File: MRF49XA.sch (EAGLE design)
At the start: 46 parts, among them J1 AVR_SPI_PRG_6NS, Q1 10Mhz, U1 ATSHA204, U2 ANT1204F002R0433A, U4 MCP73831, Y1 16MHZ

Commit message: PDF
Added PDF of the circuit.
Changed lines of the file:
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@@
 <net name="N$18" class="0">
 <segment>
-<wire x1="-121.92" y1="109.22" x2="147.32" y2="109.22" width="0.1524" layer="91"/>
-<wire x1="147.32" y1="109.22" x2="147.32" y2="10.16" width="0.1524" layer="91"/>
-<wire x1="147.32" y1="10.16" x2="-127" y2="10.16" width="0.1524" layer="91"/>
+<wire x1="-127" y1="109.22" x2="152.4" y2="109.22" width="0.1524" layer="91"/>
+<wire x1="152.4" y1="109.22" x2="152.4" y2="10.16" width="0.1524" layer="91"/>
+<wire x1="152.4" y1="10.16" x2="-127" y2="10.16" width="0.1524" layer="91"/>
 <wire x1="-127" y1="10.16" x2="-127" y2="109.22" width="0.1524" layer="91"/>
-<wire x1="-127" y1="109.22" x2="-121.92" y2="109.22" width="0.1524" layer="91"/>
 </segment>
 </net>

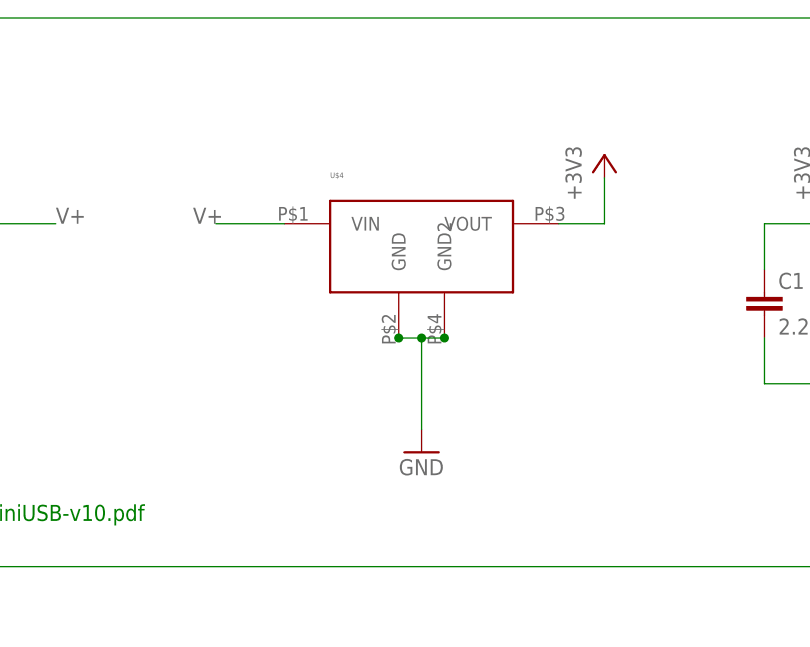
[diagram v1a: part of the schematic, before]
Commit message: Linear regulator changed
Changed it. Cheaper. Plus the other one would have blown up my circuit.
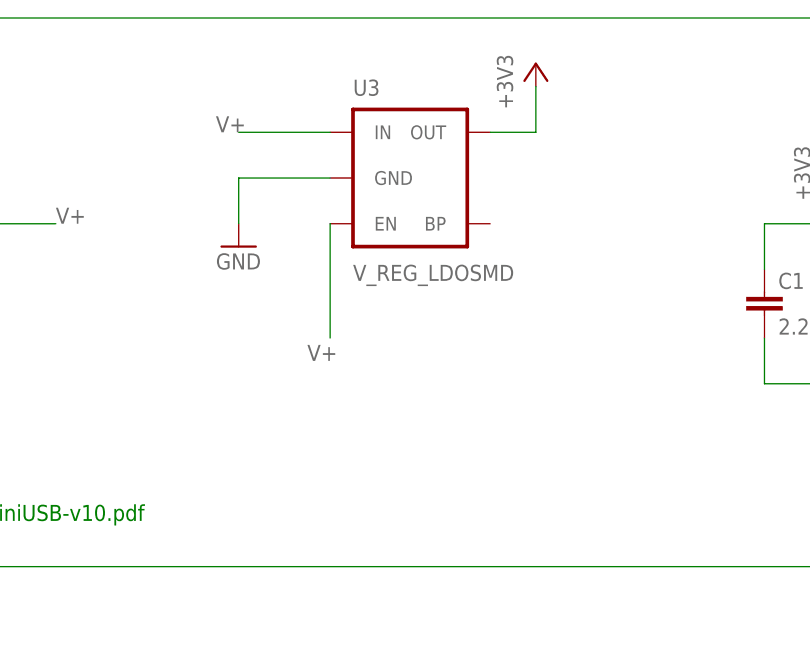
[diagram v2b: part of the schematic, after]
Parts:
- removed U$4: (no value), TestLibrary:TLV1117
- added U3: V_REG_LDOSMD, SparkFun-PowerIC:V_REG_LDOSMD
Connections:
- net +3V3: now also U3.OUT; no longer U$4.VOUT
- net GND: now also U3.GND; no longer U$4.GND, U$4.GND2
- net V+: now also U3.EN, U3.IN; no longer U$4.VIN
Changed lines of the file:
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@@
 <part name="TP3" library="testpad" deviceset="TP" device="TP08R"/>
 <part name="Y1" library="SparkFun-FreqCtrl" deviceset="RESONATOR" device="8MHZ" value="16MHZ"/>
-<part name="U$4" library="TestLibrary" deviceset="TLV1117" device=""/>
 <part name="L2" library="SparkFun-Passives" deviceset="INDUCTOR" device="0603"/>
 <part name="L1" library="SparkFun-Passives" deviceset="INDUCTOR" device="0603"/>
@@
 <part name="C9" library="SparkFun-Passives" deviceset="CAP" device="0603-CAP"/>
 <part name="U2" library="TestLibrary" deviceset="ANT1204F002R0433A" device=""/>
+<part name="U3" library="SparkFun-PowerIC" deviceset="V_REG_LDO" device="SMD"/>
 </parts>
 <sheets>
@@
 <instance part="C4" gate="G$1" x="-43.18" y="60.96"/>
 <instance part="+3V1" gate="G$1" x="83.82" y="167.64"/>
-<instance part="+3V3" gate="G$1" x="58.42" y="167.64"/>
+<instance part="+3V3" gate="G$1" x="50.8" y="177.8"/>
 <instance part="+3V4" gate="G$1" x="-66.04" y="83.82"/>
 <instance part="C8" gate="G$1" x="-50.8" y="53.34"/>
 <instance part="U$1" gate="G$1" x="-86.36" y="68.58" smashed="yes"/>
-<instance part="GND3" gate="1" x="38.1" y="134.62"/>
+<instance part="GND3" gate="1" x="17.78" y="157.48"/>
 <instance part="GND4" gate="1" x="83.82" y="134.62"/>
 <instance part="GND6" gate="1" x="-66.04" y="35.56"/>
@@
 </instance>
 <instance part="Y1" gate="G$1" x="195.58" y="53.34" rot="R270"/>
-<instance part="U$4" gate="G$1" x="40.64" y="144.78"/>
 <instance part="L2" gate="G$1" x="68.58" y="58.42"/>
 <instance part="L1" gate="G$1" x="68.58" y="78.74"/>
@@
 <instance part="C9" gate="G$1" x="91.44" y="40.64"/>
 <instance part="U2" gate="ANTENNA" x="127" y="71.12" rot="MR180"/>
+<instance part="U3" gate="G$1" x="38.1" y="165.1"/>
 </instances>
 <busses>
@@
 <segment>
 <pinref part="+3V3" gate="G$1" pin="+3V3"/>
-<wire x1="58.42" y1="165.1" x2="58.42" y2="160.02" width="0.1524" layer="91"/>
-<pinref part="U$4" gate="G$1" pin="VOUT"/>
-<wire x1="58.42" y1="160.02" x2="53.34" y2="160.02" width="0.1524" layer="91"/>
+<wire x1="50.8" y1="175.26" x2="50.8" y2="170.18" width="0.1524" layer="91"/>
+<wire x1="50.8" y1="170.18" x2="45.72" y2="170.18" width="0.1524" layer="91"/>
+<pinref part="U3" gate="G$1" pin="OUT"/>
 </segment>
 <segment>
@@
 </segment>
 <segment>
-<label x="12.7" y="160.02" size="1.778" layer="95"/>
-<pinref part="U$4" gate="G$1" pin="VIN"/>
-<wire x1="15.24" y1="160.02" x2="22.86" y2="160.02" width="0.1524" layer="91"/>
+<label x="15.24" y="170.18" size="1.778" layer="95"/>
+<wire x1="17.78" y1="170.18" x2="27.94" y2="170.18" width="0.1524" layer="91"/>
+<pinref part="U3" gate="G$1" pin="IN"/>
+</segment>
+<segment>
+<label x="25.4" y="144.78" size="1.778" layer="95"/>
+<wire x1="27.94" y1="147.32" x2="27.94" y2="160.02" width="0.1524" layer="91"/>
+<pinref part="U3" gate="G$1" pin="EN"/>
 </segment>
 </net>
@@
 </segment>
 <segment>
-<pinref part="GND3" gate="1" pin="GND"/>
-<wire x1="38.1" y1="137.16" x2="38.1" y2="147.32" width="0.1524" layer="91"/>
-<pinref part="U$4" gate="G$1" pin="GND"/>
-<pinref part="U$4" gate="G$1" pin="GND2"/>
-<wire x1="35.56" y1="147.32" x2="38.1" y2="147.32" width="0.1524" layer="91"/>
-<junction x="38.1" y="147.32"/>
-<wire x1="38.1" y1="147.32" x2="40.64" y2="147.32" width="0.1524" layer="91"/>
-<junction x="35.56" y="147.32"/>
-<junction x="40.64" y="147.32"/>
-</segment>
-<segment>
 <pinref part="C9" gate="G$1" pin="2"/>
 <wire x1="91.44" y1="38.1" x2="91.44" y2="35.56" width="0.1524" layer="91"/>
 <label x="88.9" y="33.02" size="1.778" layer="95"/>
 </segment>
+<segment>
+<pinref part="GND3" gate="1" pin="GND"/>
+<wire x1="17.78" y1="160.02" x2="17.78" y2="165.1" width="0.1524" layer="91"/>
+<pinref part="U3" gate="G$1" pin="GND"/>
+<wire x1="17.78" y1="165.1" x2="27.94" y2="165.1" width="0.1524" layer="91"/>
+</segment>
 </net>

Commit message: Capacitor and V reg
Added Aref capacitor. Changed voltage regulator.
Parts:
- added C10: 0.1uF, SparkFun-Capacitors:0.1UF-25V-5%(0603)
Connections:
- new net AREF: C10.1, U$3.AREF
- net GND: now also C10.2
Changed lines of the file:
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@@
 <part name="U2" library="TestLibrary" deviceset="ANT1204F002R0433A" device=""/>
 <part name="U3" library="SparkFun-PowerIC" deviceset="V_REG_LDO" device="SMD"/>
+<part name="C10" library="SparkFun-Capacitors" deviceset="0.1UF-25V-5%(0603)" device="" value="0.1uF"/>
+<part name="GND2" library="supply1" deviceset="GND" device=""/>
 </parts>
 <sheets>
@@
 <instance part="U2" gate="ANTENNA" x="127" y="71.12" rot="MR180"/>
 <instance part="U3" gate="G$1" x="38.1" y="165.1"/>
+<instance part="C10" gate="G$1" x="175.26" y="91.44"/>
+<instance part="GND2" gate="1" x="175.26" y="81.28"/>
 </instances>
 <busses>
@@
 <wire x1="17.78" y1="165.1" x2="27.94" y2="165.1" width="0.1524" layer="91"/>
 </segment>
+<segment>
+<pinref part="C10" gate="G$1" pin="2"/>
+<pinref part="GND2" gate="1" pin="GND"/>
+<wire x1="175.26" y1="88.9" x2="175.26" y2="83.82" width="0.1524" layer="91"/>
+</segment>
 </net>
 <net name="N$5" class="0">
@@
 </segment>
 </net>
+<net name="AREF" class="0">
+<segment>
+<pinref part="C10" gate="G$1" pin="1"/>
+<wire x1="175.26" y1="96.52" x2="175.26" y2="99.06" width="0.1524" layer="91"/>
+<label x="175.26" y="99.06" size="1.778" layer="95"/>
+</segment>
+<segment>
+<pinref part="U$3" gate="G$1" pin="AREF"/>
+<wire x1="220.98" y1="88.9" x2="215.9" y2="88.9" width="0.1524" layer="91"/>
+<label x="213.36" y="88.9" size="1.778" layer="95"/>
+</segment>
+</net>

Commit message: V Regulators
Added a list of possible voltage regulators.
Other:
- note added: "ADP1712 MIC5259 MIC5205"
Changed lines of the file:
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@@
 <text x="167.64" y="7.62" size="1.778" layer="91">Processor</text>
 <text x="119.38" y="119.38" size="1.778" layer="91">Headers &amp; Test points</text>
+<text x="25.4" y="137.16" size="1.778" layer="91">ADP1712
+MIC5259
+MIC5205</text>
 </plain>
 <instances>
@@
 </schematic>
 </drawing>
+<compatibility>
+<note version="6.3" minversion="6.2.2" severity="warning">
+Since Version 6.2.2 text objects can contain more than one line,
+which will not be processed correctly with this version.
+</note>
+</compatibility>
 </eagle>

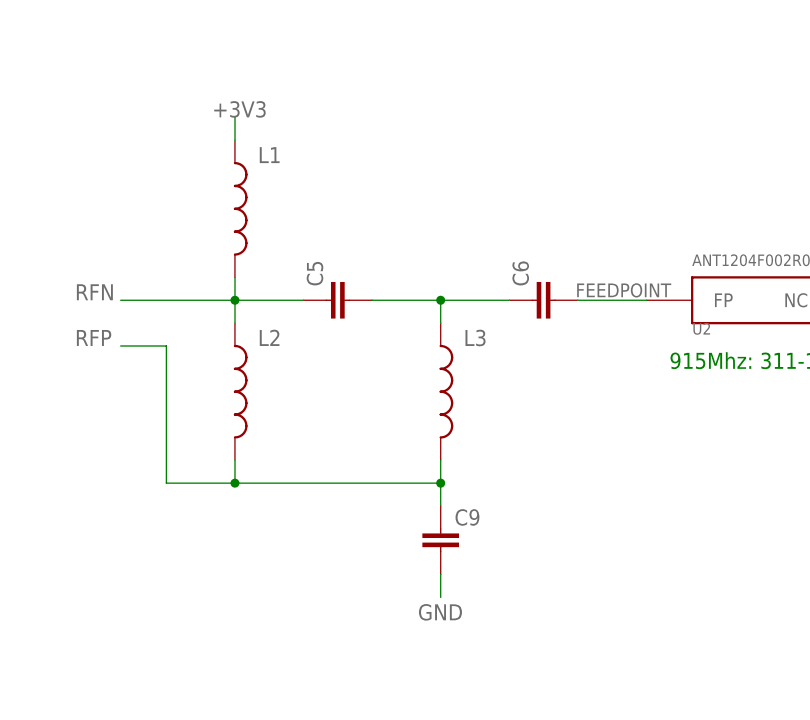
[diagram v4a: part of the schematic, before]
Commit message: BOM
Added BOM and values to antenna section
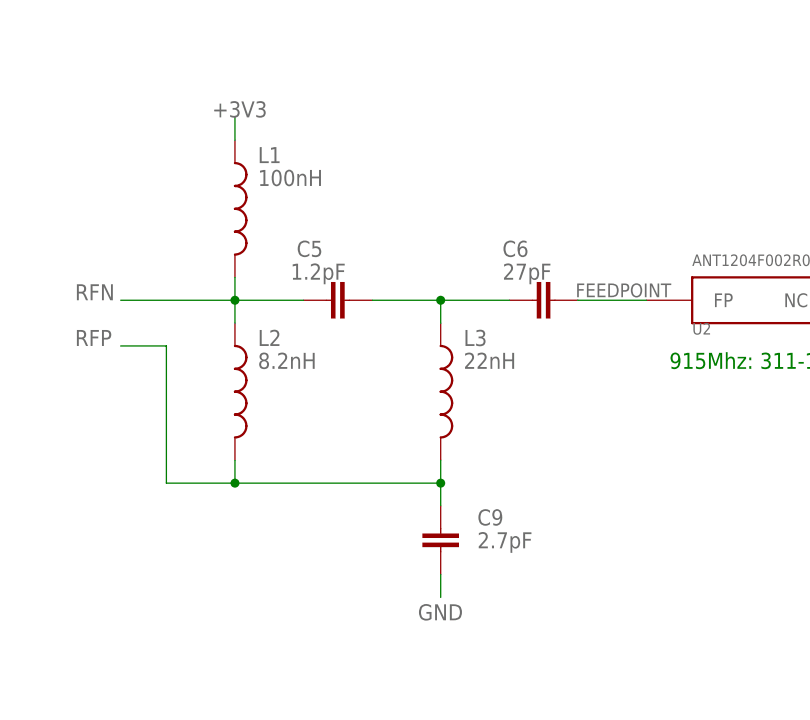
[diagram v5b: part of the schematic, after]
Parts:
- C5: value (none) -> 1.2pF
- C6: value (none) -> 27pF
- C9: value (none) -> 2.7pF
- L1: value (none) -> 100nH
- L2: value (none) -> 8.2nH
- L3: value (none) -> 22nH
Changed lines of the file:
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@@
 <part name="TP3" library="testpad" deviceset="TP" device="TP08R"/>
 <part name="Y1" library="SparkFun-FreqCtrl" deviceset="RESONATOR" device="8MHZ" value="16MHZ"/>
-<part name="L2" library="SparkFun-Passives" deviceset="INDUCTOR" device="0603"/>
-<part name="L1" library="SparkFun-Passives" deviceset="INDUCTOR" device="0603"/>
-<part name="L3" library="SparkFun-Passives" deviceset="INDUCTOR" device="0603"/>
-<part name="C5" library="SparkFun-Passives" deviceset="CAP" device="0603-CAP"/>
-<part name="C6" library="SparkFun-Passives" deviceset="CAP" device="0603-CAP"/>
-<part name="C9" library="SparkFun-Passives" deviceset="CAP" device="0603-CAP"/>
+<part name="L2" library="SparkFun-Passives" deviceset="INDUCTOR" device="0603" value="8.2nH"/>
+<part name="L1" library="SparkFun-Passives" deviceset="INDUCTOR" device="0603" value="100nH"/>
+<part name="L3" library="SparkFun-Passives" deviceset="INDUCTOR" device="0603" value="22nH"/>
+<part name="C5" library="SparkFun-Passives" deviceset="CAP" device="0603-CAP" value="1.2pF"/>
+<part name="C6" library="SparkFun-Passives" deviceset="CAP" device="0603-CAP" value="27pF"/>
+<part name="C9" library="SparkFun-Passives" deviceset="CAP" device="0603-CAP" value="2.7pF"/>
 <part name="U2" library="TestLibrary" deviceset="ANT1204F002R0433A" device=""/>
 <part name="U3" library="SparkFun-PowerIC" deviceset="V_REG_LDO" device="SMD"/>
@@
 </instance>
 <instance part="Y1" gate="G$1" x="195.58" y="53.34" rot="R270"/>
-<instance part="L2" gate="G$1" x="68.58" y="58.42"/>
-<instance part="L1" gate="G$1" x="68.58" y="78.74"/>
-<instance part="L3" gate="G$1" x="91.44" y="58.42"/>
-<instance part="C5" gate="G$1" x="81.28" y="68.58" rot="R90"/>
-<instance part="C6" gate="G$1" x="104.14" y="68.58" rot="R90"/>
-<instance part="C9" gate="G$1" x="91.44" y="40.64"/>
+<instance part="L2" gate="G$1" x="68.58" y="58.42" smashed="yes">
+<attribute name="NAME" x="71.12" y="63.5" size="1.778" layer="95"/>
+<attribute name="VALUE" x="71.12" y="60.96" size="1.778" layer="96"/>
+</instance>
+<instance part="L1" gate="G$1" x="68.58" y="78.74" smashed="yes">
+<attribute name="NAME" x="71.12" y="83.82" size="1.778" layer="95"/>
+<attribute name="VALUE" x="71.12" y="81.28" size="1.778" layer="96"/>
+</instance>
+<instance part="L3" gate="G$1" x="91.44" y="58.42" smashed="yes">
+<attribute name="NAME" x="93.98" y="63.5" size="1.778" layer="95"/>
+<attribute name="VALUE" x="93.98" y="60.96" size="1.778" layer="96"/>
+</instance>
+<instance part="C5" gate="G$1" x="81.28" y="68.58" smashed="yes" rot="R90">
+<attribute name="NAME" x="78.359" y="75.184" size="1.778" layer="95" rot="R180"/>
+<attribute name="VALUE" x="80.899" y="72.644" size="1.778" layer="96" rot="R180"/>
+</instance>
+<instance part="C6" gate="G$1" x="104.14" y="68.58" smashed="yes" rot="R90">
+<attribute name="NAME" x="101.219" y="75.184" size="1.778" layer="95" rot="R180"/>
+<attribute name="VALUE" x="103.759" y="72.644" size="1.778" layer="96" rot="R180"/>
+</instance>
+<instance part="C9" gate="G$1" x="91.44" y="40.64" smashed="yes">
+<attribute name="NAME" x="95.504" y="43.561" size="1.778" layer="95"/>
+<attribute name="VALUE" x="95.504" y="41.021" size="1.778" layer="96"/>
+</instance>
 <instance part="U2" gate="ANTENNA" x="127" y="71.12" rot="MR180"/>
 <instance part="U3" gate="G$1" x="38.1" y="165.1"/>

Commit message: More code testing
Still seeing “random” values.
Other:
- note added: "Board revisions: -Add light to pin 13 so know when it's booting -Add power switch on 3V line -Add switch to boot into bootloader"
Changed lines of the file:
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@@
 MIC5259
 MIC5205</text>
+<text x="167.64" y="-20.32" size="1.778" layer="91">Board revisions:
+-Add light to pin 13 so know when it's booting
+-Add power switch on 3V line
+-Add switch to boot into bootloader</text>
 </plain>
 <instances>
